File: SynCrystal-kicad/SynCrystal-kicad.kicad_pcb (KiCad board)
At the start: 2 copper layers, 89 x 111.8 mm, 79 parts, among them J1 ICSP, J2 Projector, Q1 SS8050, Q2 SS8050, SW1 Mode -, SW2 Mode +, SW3 Frame -, SW4 Frame +, U1 74HCT14, U2 AP2210N-3.3TRG1, U3 AP63205WU, U4 LMC6482, U5 MCP4725, U6 TS5A3160DBV, U7 ATmega328P-A, U8 ECS-TXO-3225MV-160-TR

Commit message: More Footprint work
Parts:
- added CN1: PJ-342, easyEDA:AUDIO-SMD_PJ-342, F.Cu at (39.1, 59.0)
- added J3: ~, easyEDA:HDR-SMD_HX-PM2.54-1X4P-TP-YQ, F.Cu at (76.9, 16.3)
- added J4: ~, easyEDA:HDR-SMD_HX-PM2.54-1X4P-TP-YQ, F.Cu at (133.3, 93.5)
- C10: value 100n -> 1u
- C13: value 330n -> 100n
- C14: value 100n -> 330n
- C2: value 22u -> 10u
- C3: value 22u -> 100n
- C4: value 2u2 -> 100n
- C5: value 10u -> 22u
- C6: value 100n -> 22u
- C9: value 1u -> 2u2
- D1: value Power -> SL14D; footprint LED_SMD:LED_0805_2012Metric -> Diode_SMD:D_SMA
- D2: value Crystal -> Power
- D3: value SL14D -> OLED 128x64; footprint Diode_SMD:D_SMA -> Peacemans Teile:OLED_128x63_i2c_0.96
- D4: value OLED 128x64 -> SL14D; footprint Connector_PinHeader_2.54mm:PinHeader_1x04_P2.54mm_Vertical -> Diode_SMD:D_SMA
- D5: value Ext. Imp. -> SL14D; footprint LED_SMD:LED_0805_2012Metric -> Diode_SMD:D_SMA
- D6: value SL14D -> in sync; footprint Diode_SMD:D_SMA -> LED_SMD:LED_0805_2012Metric
- D7: value in sync -> Crystal
- D8: value SL14D -> Ext. Imp.; footprint Diode_SMD:D_SMA -> LED_SMD:LED_0805_2012Metric
- J2: footprint Connector_PinHeader_2.54mm:PinHeader_1x04_P2.54mm_Horizontal -> easyEDA:CONN-TH_S4B-PH-KL-LF-SN
- R1: value 3k3 -> 2k2
- R10: value 10k -> 4k7
- R11: value 4k7 -> 3k3
- R13: value 2k2 -> 10k
- R15: value 2k2 -> 3k3
- R16, R18: value 10k -> 100k
- R17: value 1k -> 5k6
- R19: value 10k -> 47
- R2: value 47k -> 2k2
- R20: value 100k -> 10k
- R21: value 100k -> 3K3
- R22: value 100K -> 3K3
- R23: value 47 -> 1k
- R24: value 3K3 -> 100K
- R3: value 470k -> 10k
- R4: value 3k3 -> 3K3
- R5: value 3K3 -> 10k
- R7: value 3K3 -> 47k
- R8: value 12k -> 470k
- R9: value 5k6 -> 12k
- RV1: footprint easyEDA:RES-TH_RK09K1110A0J_short -> easyEDA:RES-SMD_RK10J11R0A0H
- SW1, SW2, SW3, SW4: footprint Button_Switch_SMD:SW_Push_1P1T_NO_6x6mm_H9.5mm -> Button_Switch_SMD:SW_SPST_PTS647_Sx50
- TP1: value 5V -> P
- TP10: value Pulse Out -> Imp IN
- TP2: value 3V3 -> I
- TP3: value DAC -> D
- TP4: value P -> Rx
- TP5: value I -> Tx
- TP6: value D -> Pulse Out
- TP7: value Rx -> 5V
- TP8: value Tx -> 3V3
- TP9: value Imp IN -> DAC
- U2: value AP2210N-3.3TRG1 -> ATmega328P-A; footprint Package_TO_SOT_SMD:SOT-23-3 -> Package_QFP:TQFP-32_7x7mm_P0.8mm
- U4: value LMC6482 -> ECS-TXO-3225MV-160-TR; footprint Package_SO:SOIC-8_3.9x4.9mm_P1.27mm -> Crystal:Crystal_SMD_3225-4Pin_3.2x2.5mm
- U5: value MCP4725 -> AP2210N-3.3TRG1; footprint Package_TO_SOT_SMD:SOT-23-6 -> Package_TO_SOT_SMD:SOT-23-3
- U6: value TS5A3160DBV -> MCP4725
- U7: value ATmega328P-A -> TS5A3160DBV; footprint Package_QFP:TQFP-32_7x7mm_P0.8mm -> Package_TO_SOT_SMD:SOT-23-6
- U8: value ECS-TXO-3225MV-160-TR -> LMC6482; footprint Crystal:Crystal_SMD_3225-4Pin_3.2x2.5mm -> Package_SO:SOIC-8_3.9x4.9mm_P1.27mm
- moved C10 140.2 mm to (182.7, 65.0)
- moved C11 140.2 mm to (207.4, 76.3)
- moved C12 140.2 mm to (215.3, 71.9)
- moved C13 140.2 mm to (213.3, 71.9)
- moved C14 140.2 mm to (203.0, 57.7)
- moved C15 140.2 mm to (200.9, 68.1)
- moved C6 140.2 mm to (195.3, 69.7)
- moved C8 140.2 mm to (195.3, 78.6)
- moved C9 140.2 mm to (188.7, 77.8)
- moved Q1 140.2 mm to (201.0, 71.7)
- moved Q2 140.2 mm to (218.6, 75.6)
- moved R1 140.2 mm to (197.8, 69.7)
- moved R10 140.2 mm to (188.8, 85.4)
- moved R11 140.2 mm to (187.8, 83.1)
- moved R12 140.2 mm to (189.6, 83.1)
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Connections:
- C1 pad 1: Net-(U3-SW) -> Net-(U2-AREF)
- C1 pad 2: Net-(U3-BST) -> GND
- C10 pad 1: Net-(U7-AREF) -> GND
- C10 pad 2: GND -> +5V
- C11 pad 1: Net-(D3-A) -> +5V
- C11 pad 2: Net-(U4B-+) -> GND
- C12 pad 1: Net-(Q2-B) -> Net-(C12-Pad1)
- C12 pad 2: /INT1 -> GND
- C13 pad 1: GND -> Net-(D4-A)
- C13 pad 2: Net-(C13-Pad2) -> Net-(U8B-+)
- C14 pad 1: +3.3V -> GND
- C14 pad 2: GND -> Net-(C14-Pad2)
- C15 pad 1: GND -> Net-(Q2-B)
- C15 pad 2: +5V -> /INT1
- C2 pad 1: +5V -> Net-(D1-K)
- C3 pad 1: +5V -> Net-(U3-SW)
- C3 pad 2: GND -> Net-(U3-BST)
- C5 pad 1: Net-(D8-K) -> +5V
- C6 pad 1: Net-(C6-Pad1) -> +5V
- C8 pad 1: +5V -> GND
- C8 pad 2: GND -> +5V
- C9 pad 1: GND -> +3.3V
- C9 pad 2: +5V -> GND
- D1 pad 1: GND -> Net-(D1-K)
- D1 pad 2: Net-(D1-A) -> /Proj_Vcc
- D3 pad 1: +5V -> Net-(D3-GND)
- D3 pad 2: Net-(D3-A) -> Net-(D3-VCC)
- D4 pad 1: Net-(D4-GND) -> +5V
- D4 pad 2: Net-(D4-VCC) -> Net-(D4-A)
- D5 pad 1: GND -> Net-(D4-A)
- D5 pad 2: Net-(D5-A) -> GND
- D6 pad 1: Net-(D3-A) -> Net-(D6-K)
- D6 pad 2: GND -> Net-(D6-A)
- D7 pad 1: GND -> Net-(D6-K)
- D8 pad 1: Net-(D8-K) -> Net-(D6-K)
- D8 pad 2: /Proj_Vcc -> Net-(D8-A)
- JP1 pad 1: Net-(D4-VCC) -> Net-(D3-VCC)
- JP2 pad 1: Net-(D4-GND) -> Net-(D3-GND)
- JP2 pad 3: Net-(D4-VCC) -> Net-(D3-VCC)
- Q2 pad 3: Net-(Q2-C) -> /Ext_Imp_LED
- R1 pad 1: Net-(Q1-C) -> /SDA
- R10 pad 1: Net-(U4A--) -> GND
- R10 pad 2: Net-(U5-VOUT) -> Net-(U8A-+)
- R11 pad 1: GND -> Net-(Q1-C)
- R11 pad 2: Net-(U4A-+) -> +5V
- R12 pad 2: Net-(U4A--) -> Net-(U8A--)
- R13 pad 1: Net-(R13-Pad1) -> Net-(D4-A)
- R13 pad 2: Net-(R12-Pad1) -> Net-(R13-Pad2)
- R14 pad 1: /SDA -> Net-(R14-Pad1)
- R14 pad 2: +5V -> Net-(R12-Pad1)
- R15 pad 1: +5V -> Net-(R15-Pad1)
- R15 pad 2: /SCL -> Net-(C12-Pad1)
- R16 pad 1: +5V -> GND
- R16 pad 2: /~{RST} -> Net-(D4-A)
- R17 pad 1: Net-(D5-A) -> Net-(R14-Pad1)
- R17 pad 2: Net-(Q2-C) -> Net-(R17-Pad2)
- R18 pad 1: Net-(D3-A) -> GND
- R18 pad 2: Net-(R18-Pad2) -> Net-(U8B-+)
- R19 pad 1: Net-(C13-Pad2) -> Net-(R19-Pad1)
- R19 pad 2: Net-(R19-Pad2) -> GND
- R2 pad 2: Net-(Q1-B) -> /SCL
- R20 pad 1: GND -> Net-(C14-Pad2)
- R20 pad 2: Net-(D3-A) -> Net-(R20-Pad2)
- R21 pad 1: GND -> Net-(J4-Pin_1)
- R21 pad 2: Net-(U4B-+) -> Net-(D6-A)
- R22 pad 1: Net-(Q2-B) -> Net-(J4-Pin_2)
- R22 pad 2: GND -> Net-(D7-A)
- R23 pad 1: Net-(R23-Pad1) -> Net-(D8-A)
- R23 pad 2: GND -> Net-(J4-Pin_3)
- R24 pad 1: Net-(U7-PD5) -> Net-(Q2-B)
- R24 pad 2: Net-(D7-A) -> GND
- R3 pad 1: Net-(Q1-B) -> +5V
- R3 pad 2: Net-(Q1-C) -> /~{RST}
- R4 pad 1: Net-(R4-Pad1) -> +5V
- R4 pad 2: Net-(C6-Pad1) -> Net-(D2-A)
- R5 pad 1: +5V -> /M-Pin
- R5 pad 2: Net-(D1-A) -> Net-(Q1-B)
- R6 pad 1: /M-Pin -> Net-(U8A--)
- R6 pad 2: Net-(Q1-B) -> Net-(U6-VOUT)
- R7 pad 1: Net-(D2-A) -> +5V
- R7 pad 2: /DAC_EN -> Net-(Q1-B)
- R8 pad 1: Net-(U4A-+) -> Net-(Q1-B)
- R8 pad 2: +5V -> Net-(Q1-C)
- R9 pad 1: Net-(R13-Pad1) -> Net-(U8A-+)
- R9 pad 2: Net-(R9-Pad2) -> +5V
- RV1 pad 1: Net-(R23-Pad1) -> Net-(R19-Pad1)
- RV1 pad 2: Net-(U4B--) -> Net-(U8B--)
- RV1 pad 3: Net-(R19-Pad2) -> Net-(R20-Pad2)
- TP1 pad 1: +5V -> /P_POT
- TP10 pad 1: Net-(U7-PD7) -> Net-(R13-Pad2)
- TP2 pad 1: +3.3V -> /I_POT
- TP3 pad 1: Net-(U5-VOUT) -> /D_POT
- TP4 pad 1: /P_POT -> /RX
- TP5 pad 1: /I_POT -> /TX
- TP6 pad 1: /D_POT -> Net-(U2-PD7)
- TP7 pad 1: /RX -> +5V
- TP8 pad 1: /TX -> +3.3V
- TP9 pad 1: Net-(R18-Pad2) -> Net-(U6-VOUT)
- U1 pad 1: Net-(C13-Pad2) -> Net-(C14-Pad2)
- U1 pad 11: Net-(C6-Pad1) -> Net-(C12-Pad1)
- U1 pad 12: Net-(R4-Pad1) -> Net-(R15-Pad1)
- U1 pad 3: Net-(U8-Output) -> Net-(U4-Output)
- U2 pad 1: GND -> /INT1
- U2 pad 2: +3.3V -> /Frame-
- U2 pad 3: +5V -> GND
- U3 pad 2: Net-(D8-K) -> Net-(D1-K)
- U3 pad 3: Net-(D8-K) -> Net-(D1-K)
- U4 pad 1: Net-(R13-Pad1) -> unconnected-(U4-Tri-State-Pad1)
- U4 pad 2: Net-(U4A--) -> GND
- U4 pad 3: Net-(U4A-+) -> Net-(U4-Output)
- U4 pad 4: GND -> +3.3V
- U5 pad 1: Net-(U5-VOUT) -> GND
- U5 pad 2: GND -> +3.3V
- U6 pad 1: Net-(R9-Pad2) -> Net-(U6-VOUT)
- U6 pad 3: unconnected-(U6-Pad3) -> +5V
- U6 pad 4: /Pin 6-7-8 -> /SDA
- U6 pad 5: +5V -> /SCL
- U6 pad 6: /DAC_EN -> GND
- U7 pad 1: /INT1 -> Net-(R17-Pad2)
- U7 pad 2: /Frame- -> GND
- U7 pad 3: GND -> unconnected-(U7-Pad3)
- U7 pad 4: +5V -> /Pin 6-7-8
- U7 pad 5: GND -> +5V
- U7 pad 6: +5V -> /Crystal_LED
- U8 pad 1: unconnected-(U8-Tri-State-Pad1) -> Net-(R14-Pad1)
- U8 pad 2: GND -> Net-(U8A--)
- U8 pad 3: Net-(U8-Output) -> Net-(U8A-+)
- U8 pad 4: +3.3V -> GND
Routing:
- net (no net): track 0.00 -> 31.6 mm
- net +5V: track 35.8 -> 52.5 mm, vias 9 -> 10
- net Net-(R9-Pad2): track 11.1 -> 0.00 mm, vias 2 -> 0
- net Net-(U4A-+): track 10.1 -> 0.00 mm
- net Net-(U5-VOUT): track 7.47 -> 0.00 mm
- net Net-(U4A--): track 5.46 -> 0.00 mm
- net GND: track 11.5 -> 16.6 mm, vias 0 -> 1
- net Net-(R13-Pad1): track 4.74 -> 0.00 mm
- net Net-(D8-K): track 4.19 -> 0.00 mm
- net Net-(C6-Pad1): track 3.85 -> 0.00 mm
- net /SCL: track 3.11 -> 0.00 mm
- net Net-(U8-Output): track 2.07 -> 0.00 mm
- net Net-(U4-Output): track 0.00 -> 2.07 mm
- net Net-(R4-Pad1): track 2.02 -> 0.00 mm
- net /DAC_EN: track 1.43 -> 0.00 mm
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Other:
- board text added: "UI Anordnen Elektronik drumrum LED an Bus Ess an Bus?"

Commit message: More schematics
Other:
- board text added: "UI Anordnen ESS an Bus?"
- board text removed: "UI Anordnen Elektronik drumrum LED an Bus Ess an Bus?"
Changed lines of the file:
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@@
 		(layer "Edge.Cuts")
 	)
-	(gr_text "UI Anordnen\nElektronik drumrum\nLED an Bus\nEss an Bus?\n"
+	(gr_text "UI Anordnen\nESS an Bus?\n"
 		(at 132.842 40.132 0)
 		(layer "F.Cu")

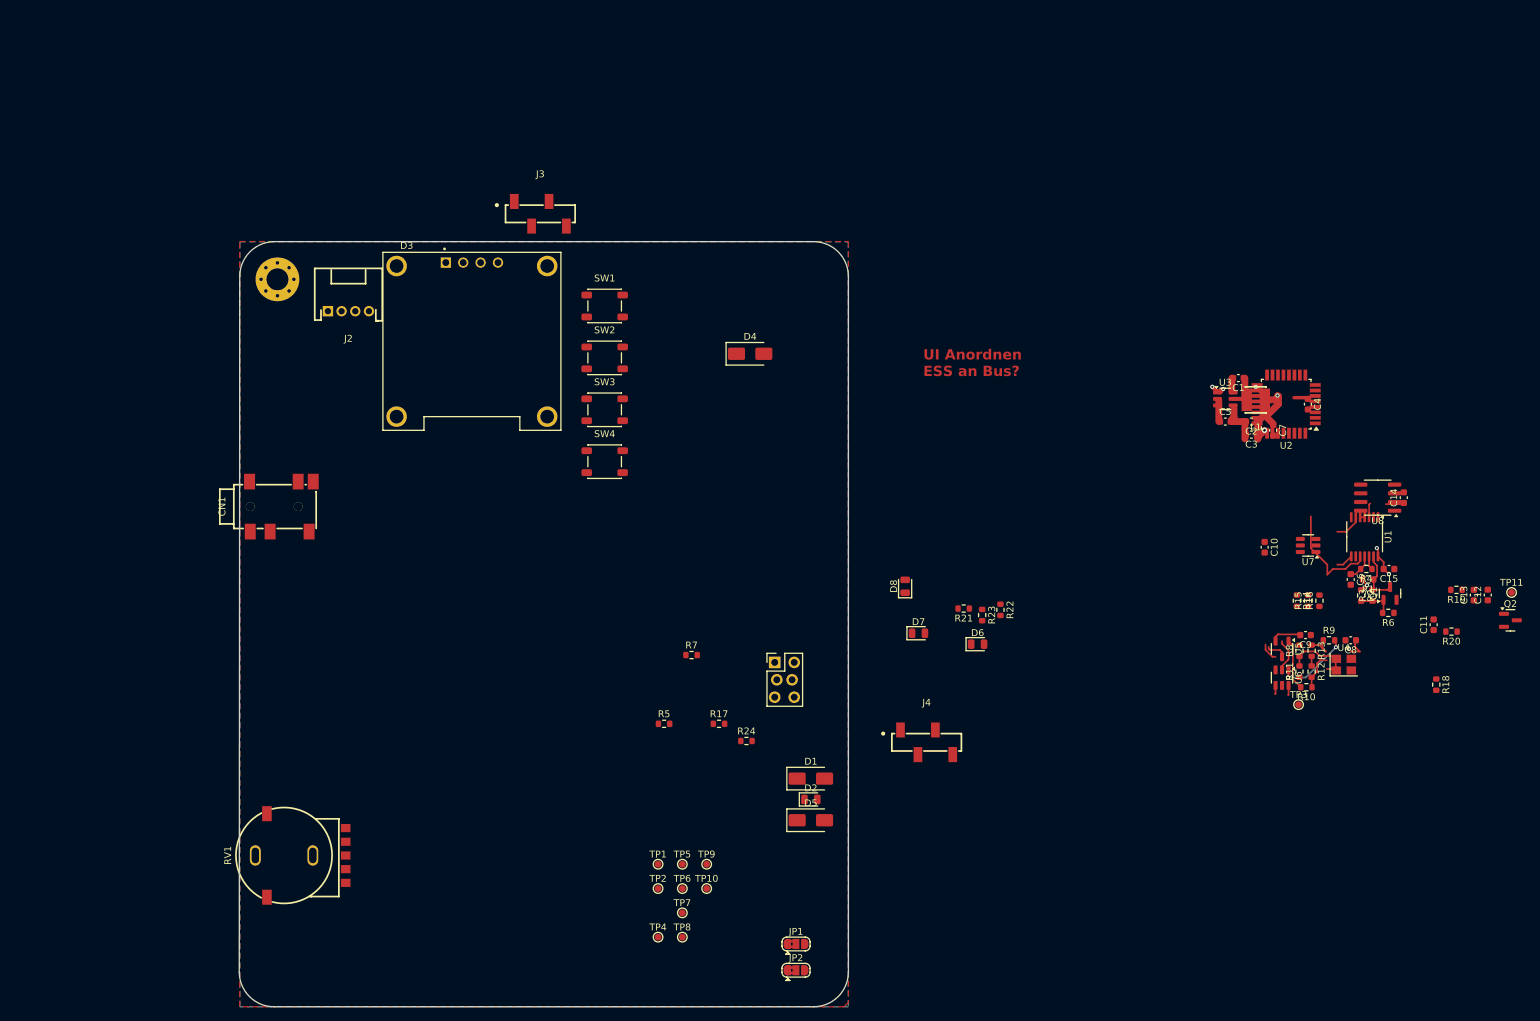
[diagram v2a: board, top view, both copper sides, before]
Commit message: Adding the VOltage Divider to Projector Board to allow Projector Detection. Also, fixing various footprints on the controller. ERC now failing.
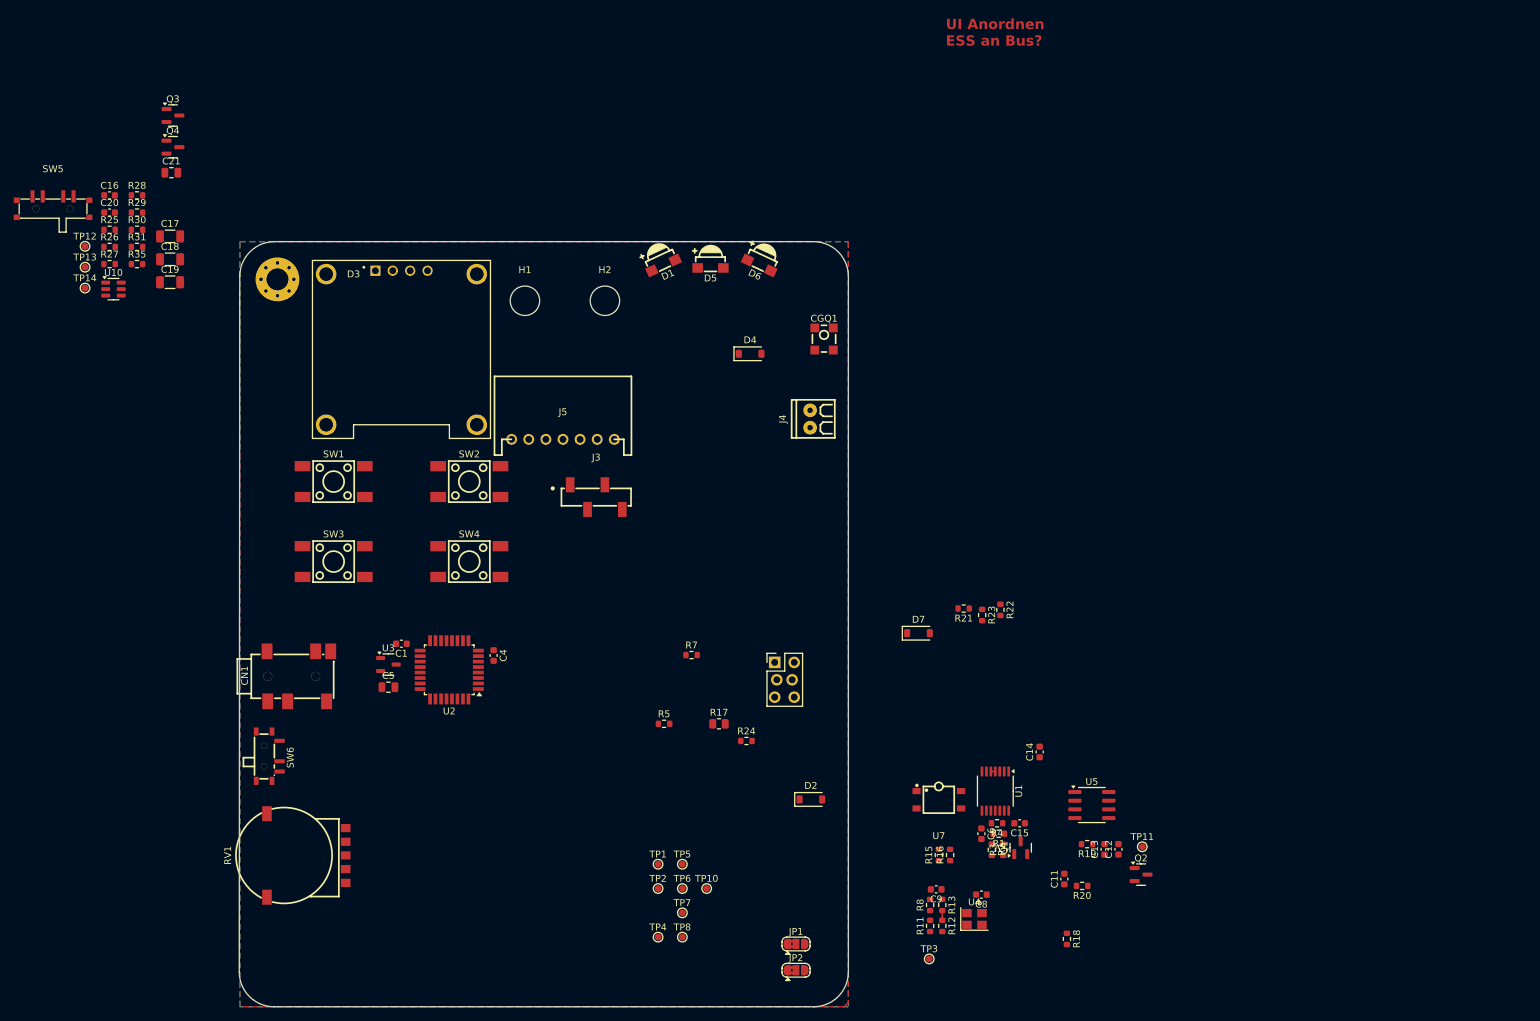
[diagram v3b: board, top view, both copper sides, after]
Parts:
- removed C10, C7: 1u, Capacitor_SMD:C_0603_1608Metric
- removed C2: 10u, Capacitor_SMD:C_0603_1608Metric
- removed C3: 100n, Capacitor_SMD:C_0603_1608Metric
- removed D8: Ext. Imp., LED_SMD:LED_0805_2012Metric
- removed J2: Projector, easyEDA:CONN-TH_S4B-PH-KL-LF-SN
- removed L1: 4.7uH, easyEDA:IND-SMD_L3.0-W3.0
- removed R10: 4k7, Resistor_SMD:R_0603_1608Metric
- removed R14: 2k2, Resistor_SMD:R_0603_1608Metric
- removed R6: 10k, Resistor_SMD:R_0603_1608Metric
- removed R9: 12k, Resistor_SMD:R_0603_1608Metric
- removed TP9: DAC, TestPoint:TestPoint_Pad_D1.0mm
- removed U6: MCP4725, Package_TO_SOT_SMD:SOT-23-6
- removed U8: LMC6482, Package_SO:SOIC-8_3.9x4.9mm_P1.27mm
- added C16: 100n, Capacitor_SMD:C_0603_1608Metric, F.Cu at (14.0, 13.6)
- added C17: 47u, Capacitor_SMD:C_1206_3216Metric, F.Cu at (22.8, 19.6)
- added C18: 47u, Capacitor_SMD:C_1206_3216Metric, F.Cu at (22.8, 22.9)
- added C19: 47u, Capacitor_SMD:C_1206_3216Metric, F.Cu at (22.8, 26.3)
- added C20: 2u2, Capacitor_SMD:C_0603_1608Metric, F.Cu at (14.0, 16.1)
- added C21: 22u, Capacitor_SMD:C_0805_2012Metric, F.Cu at (23.0, 10.3)
- added CGQ1: DY-IRMHF384-T05-2.5KB, easyEDA:OPTO-SMD_4P-L3.9-W3.4_IRM-H432M3-R8, F.Cu at (118.4, 34.5)
- added H1: MountingHole, MountingHole:MountingHole_4.3mm_M4_ISO14580, F.Cu at (74.7, 29.0)
- added H2: MountingHole, MountingHole:MountingHole_4.3mm_M4_ISO14580, F.Cu at (86.4, 29.0)
- added J5: to DIN-6 Male, easyEDA:CONN-TH_S7B-XH-A-LF-SN, F.Cu at (80.2, 49.2)
- added Q3: AO3400A, Package_TO_SOT_SMD:SOT-23, F.Cu at (23.3, 1.90)
- added Q4: SS8050, Package_TO_SOT_SMD:SOT-23, F.Cu at (23.3, 6.53)
- added R25: 100k, Resistor_SMD:R_0603_1608Metric, F.Cu at (14.0, 18.6)
- added R26: 100k, Resistor_SMD:R_0603_1608Metric, F.Cu at (14.0, 21.1)
- added R27: 10k, Resistor_SMD:R_0603_1608Metric, F.Cu at (14.0, 23.6)
- added R28: 470, Resistor_SMD:R_0603_1608Metric, F.Cu at (18.0, 13.6)
- added R29: 100k, Resistor_SMD:R_0603_1608Metric, F.Cu at (18.0, 16.1)
- added R30: 10k, Resistor_SMD:R_0603_1608Metric, F.Cu at (18.0, 18.6)
- added R31: 47, Resistor_SMD:R_0603_1608Metric, F.Cu at (18.0, 21.1)
- added R35: 220k, Resistor_SMD:R_0603_1608Metric, F.Cu at (18.0, 23.6)
- added SW5: Shaft_Pulse_Ratio, easyEDA:SW-SMD_MSK13C02-SZ, F.Cu at (5.75, 15.2)
- added SW6: Guide/Follow, easyEDA:SW-TH_MSK12C02-HB-1, F.Cu at (37.1, 95.5)
- added TP12: DAC, TestPoint:TestPoint_Pad_D1.0mm, F.Cu at (10.4, 21.0)
- added TP13: Pause, TestPoint:TestPoint_Pad_D1.0mm, F.Cu at (10.4, 24.1)
- added TP14: Pause, TestPoint:TestPoint_Pad_D1.0mm, F.Cu at (10.4, 27.1)
- added U10: MCP4725, Package_TO_SOT_SMD:SOT-23-6, F.Cu at (14.6, 27.3)
- C11: value 100n -> 1u
- C14: value 330n -> 100n
- C15: value 100n -> 330n
- C5: footprint Capacitor_SMD:C_0603_1608Metric -> Capacitor_SMD:C_0805_2012Metric
- C6: value 22u -> 2u2
- C9: value 2u2 -> 1u
- D1, D5: value SL14D -> LED; footprint Diode_SMD:D_SMA -> easyEDA:LED-SMD_XYC-IRA4335A65-X4
- D2: value Power -> B5819W SL; footprint LED_SMD:LED_0805_2012Metric -> Diode_SMD:D_SOD-123
- D4: value SL14D -> B5819W SL; footprint Diode_SMD:D_SMA -> Diode_SMD:D_SOD-123
- D6: value in sync -> LED; footprint LED_SMD:LED_0805_2012Metric -> easyEDA:LED-SMD_XYC-IRA4335A65-X4
- D7: value Crystal -> B5819W SL; footprint LED_SMD:LED_0805_2012Metric -> Diode_SMD:D_SOD-123
- J4: value ~ -> Pause Button; footprint easyEDA:HDR-SMD_HX-PM2.54-1X4P-TP-YQ -> easyEDA:CONN-TH_2P-P2.54_MX128-2.54-GN01-02P-CU-Y-A
- R12: value 100 -> 100k
- R15: value 3k3 -> 10k
- R16: value 100k -> 10k
- R17: value 5k6 -> 5R1; footprint Resistor_SMD:R_0603_1608Metric -> Resistor_SMD:R_0805_2012Metric
- R19: value 47 -> 100k
- R20: value 10k -> 100k
- R21: value 3K3 -> 47
- R22: value 3K3 -> 10
- R23: value 1k -> 22k
- R24: value 100K -> 100
- R4: value 3K3 -> 220k
- R5: value 10k -> 3k3
- RV1: footprint easyEDA:RES-SMD_RK10J11R0A0H -> easyEDA:RES-SMD_RK10J11R0A0H_fixed
- SW1, SW2, SW3, SW4: footprint Button_Switch_SMD:SW_SPST_PTS647_Sx50 -> easyEDA:SW-SMD_4P-L6.0-W6.0-P4.50-LS9.0_TS-1002S-08026C
- TP6: value Pulse Out -> fps pulse
- U3: value AP63205WU -> AP2210N-3.3TRG1; footprint Package_TO_SOT_SMD:TSOT-23-6 -> Package_TO_SOT_SMD:SOT-23-3
- U5: value AP2210N-3.3TRG1 -> LMC6482; footprint Package_TO_SOT_SMD:SOT-23-3 -> Package_SO:SOIC-8_3.9x4.9mm_P1.27mm
- U7: value TS5A3160DBV -> G3VM-61VY3(TR); footprint Package_TO_SOT_SMD:SOT-23-6 -> easyEDA:SOP-4_L3.9-W4.4-P2.54-LS7.0-BR
- moved C5 128.3 mm to (54.7, 85.4)
- moved U3 128.3 mm to (54.7, 82.1)
- moved C1 128.3 mm to (56.6, 79.1)
- moved U2 128.3 mm to (63.6, 82.9)
- moved C4 124.5 mm to (70.1, 80.8)
- moved D5 82.0 mm to (101.8, 24.2)
- moved D1 78.0 mm to (94.9, 23.8), turned to 25 degrees
- moved R15 65.5 mm to (135.1, 109.9)
- moved R20 65.5 mm to (156.1, 114.4)
- moved C11 65.5 mm to (153.5, 113.4)
- moved C13 65.5 mm to (159.3, 109.1)
- moved Q1 65.5 mm to (147.1, 108.9)
- moved R1 65.5 mm to (143.9, 106.8)
- moved R11 65.5 mm to (133.9, 120.3)
- moved R12 65.5 mm to (135.6, 120.3)
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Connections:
- C11 pad 1: +5V -> GND
- C11 pad 2: GND -> +5V
- C12 pad 1: Net-(C12-Pad1) -> GND
- C12 pad 2: GND -> +5V
- C13 pad 1: Net-(D4-A) -> Net-(D2-A)
- C13 pad 2: Net-(U8B-+) -> Net-(U5B-+)
- C14 pad 1: GND -> Net-(Q2-B)
- C14 pad 2: Net-(C14-Pad2) -> /INT1
- C15 pad 1: Net-(Q2-B) -> GND
- C15 pad 2: /INT1 -> Net-(C15-Pad2)
- C6 pad 1: +5V -> +3.3V
- C8 pad 1: GND -> Net-(C8-Pad1)
- C8 pad 2: +5V -> GND
- C9 pad 1: +3.3V -> +5V
- CN1 pad 2: unconnected-(CN1-Pad2) -> GND
- CN1 pad 3: unconnected-(CN1-Pad3) -> GND
- CN1 pad 5: unconnected-(CN1-Pad5) -> Net-(CN1-Pad5)
- CN1 pad 6: unconnected-(CN1-Pad6) -> GND
- CN1 pad 7: unconnected-(CN1-Pad7) -> GND
- D1 pad 1: Net-(D1-K) -> Net-(D1-A)
- D1 pad 2: /Proj_Vcc -> Net-(D1-K)
- D2 pad 1: GND -> +5V
- D4 pad 1: +5V -> Net-(D2-A)
- D4 pad 2: Net-(D4-A) -> GND
- D5 pad 1: Net-(D4-A) -> Net-(D5-K)
- D5 pad 2: GND -> Net-(D1-A)
- D6 pad 2: Net-(D6-A) -> Net-(D5-K)
- D7 pad 1: Net-(D6-K) -> Net-(D7-K)
- J3 pad 2: /Crystal_LED -> /DAC_EN
- R11 pad 1: Net-(Q1-C) -> Net-(R11-Pad1)
- R11 pad 2: +5V -> Net-(C8-Pad1)
- R12 pad 1: Net-(R12-Pad1) -> +5V
- R12 pad 2: Net-(U8A--) -> /Stop_EN
- R13 pad 1: Net-(D4-A) -> Net-(D2-A)
- R13 pad 2: Net-(R13-Pad2) -> Net-(CN1-Pad5)
- R15 pad 1: Net-(R15-Pad1) -> /M-Pin
- R15 pad 2: Net-(C12-Pad1) -> Net-(Q1-B)
- R16 pad 1: GND -> Net-(C15-Pad2)
- R16 pad 2: Net-(D4-A) -> Net-(R16-Pad2)
- R17 pad 1: Net-(R14-Pad1) -> +5V
- R17 pad 2: Net-(R17-Pad2) -> Net-(D1-K)
- R18 pad 2: Net-(U8B-+) -> Net-(D2-A)
- R19 pad 1: Net-(R19-Pad1) -> GND
- R19 pad 2: GND -> Net-(U5B-+)
- R20 pad 1: Net-(C14-Pad2) -> Net-(Q2-B)
- R20 pad 2: Net-(R20-Pad2) -> GND
- R21 pad 1: Net-(J4-Pin_1) -> Net-(R21-Pad1)
- R21 pad 2: Net-(D6-A) -> GND
- R22 pad 1: Net-(J4-Pin_2) -> /IRSEND
- R22 pad 2: Net-(D7-A) -> Net-(Q3-G)
- R23 pad 1: Net-(D8-A) -> /IRSEND
- R23 pad 2: Net-(J4-Pin_3) -> GND
- R24 pad 1: Net-(Q2-B) -> Net-(D7-A)
- R24 pad 2: GND -> /IRSEND
- R4 pad 2: Net-(D2-A) -> Net-(SW6-A)
- R5 pad 1: /M-Pin -> Net-(Q1-C)
- R5 pad 2: Net-(Q1-B) -> +5V
- RV1 pad 1: Net-(R19-Pad1) -> Net-(R21-Pad1)
- RV1 pad 2: Net-(U8B--) -> Net-(U5B--)
- RV1 pad 3: Net-(R20-Pad2) -> Net-(R16-Pad2)
- SW1 pad 1: GND -> unconnected-(SW1-Pad1)
- SW2 pad 1: GND -> unconnected-(SW2-Pad1)
- SW3 pad 1: GND -> unconnected-(SW3-Pad1)
- SW4 pad 1: GND -> unconnected-(SW4-Pad1)
- TP10 pad 1: Net-(R13-Pad2) -> Net-(CN1-Pad5)
- TP6 pad 1: Net-(U2-PD7) -> /MOSI
- U1 pad 1: Net-(C14-Pad2) -> Net-(C15-Pad2)
- U1 pad 11: Net-(C12-Pad1) -> Net-(C8-Pad1)
- U1 pad 12: Net-(R15-Pad1) -> Net-(R11-Pad1)
- U2 pad 11: Net-(U2-PD7) -> /Stop_EN
- U2 pad 13: /Crystal_LED -> /DAC_EN
- U2 pad 19: unconnected-(U2-ADC6-Pad19) -> /P_POT
- U2 pad 22: unconnected-(U2-ADC7-Pad22) -> /I_POT
- U2 pad 23: /P_POT -> Net-(U2-PC0)
- U2 pad 24: /I_POT -> /IRSEND
- U3 pad 1: +5V -> GND
- U3 pad 2: Net-(D1-K) -> +3.3V
- U3 pad 3: Net-(D1-K) -> +5V
- U5 pad 1: GND -> Net-(U5A--)
- U5 pad 2: +3.3V -> Net-(U5A--)
- U5 pad 3: +5V -> GND
- U7 pad 1: Net-(R17-Pad2) -> Net-(R28-Pad2)
- U7 pad 3: unconnected-(U7-Pad3) -> Net-(J4-Pin_2)
- U7 pad 4: /Pin 6-7-8 -> Net-(J4-Pin_1)
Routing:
- net +5V: track 52.5 -> 1.58 mm, vias 10 -> 0
- net (no net): track 31.6 -> 0.00 mm
- net GND: track 16.6 -> 0.00 mm, vias 1 -> 0
- net /INT0: track 15.8 -> 0.00 mm
- net Net-(Q1-C): track 8.11 -> 0.00 mm
- net Net-(Q1-B): track 5.30 -> 0.00 mm
- net Net-(U3-SW): track 5.23 -> 0.00 mm
- net +3.3V: track 4.65 -> 0.27 mm
- net /uC-Clock: track 4.02 -> 0.00 mm
- net /SDA: track 3.94 -> 0.00 mm
- net /INT1: track 2.56 -> 0.00 mm
- net Net-(U3-BST): track 2.17 -> 0.00 mm
- net Net-(U4-Output): track 2.07 -> 0.00 mm
- net Net-(R12-Pad1): track 1.40 -> 0.00 mm
- net Net-(C8-Pad1): vias 0 -> 1
